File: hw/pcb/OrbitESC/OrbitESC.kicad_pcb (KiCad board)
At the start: 4 copper layers, 58 x 30 mm, 143 parts, among them J1 USB_C_Receptacle_USB2.0, J11 VDC, J12 GND, J3 TermA, J4 TermB, J5 TermC, J6 CAN1, Q1 MCAC80N10Y, Q2 MCAC80N10Y, Q3 MCAC80N10Y, Q4 MCAC80N10Y, Q5 MCAC80N10Y, Q6 MCAC80N10Y, Q7 2N7002, SW1 Reset, SW2 Boot, U1 TLE9250X, U10 CP2104, U11 STM32L432KBUx, U2 AT25SF081-SSHD-X, U3 24LC128, U4 74HC596, U5 DRV8300DRGER, U6 TSV994, U7 AP62200Z6-7, U8 AP2171W, U9 AP2120

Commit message: PCB cleanup
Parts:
- C10, C13, C4, C7, R15, R19, R20, R23, R24, U10: moved to F.Cu
- R9: moved to B.Cu
- moved D5 53.0 mm to (173.8, 71.3)
- moved D16 50.2 mm to (168.8, 69.4)
- moved D17 50.2 mm to (168.8, 71.7)
- moved D19 50.2 mm to (168.8, 74.0)
- moved R87 50.2 mm to (170.5, 69.4)
- moved R88 50.2 mm to (170.5, 71.7)
- moved R90 50.2 mm to (170.5, 74.0)
- moved SW2 42.4 mm to (155.2, 69.5)
- moved U2 41.8 mm to (156.0, 63.7)
- moved SW1 41.5 mm to (161.7, 70.6)
- moved R29 38.1 mm to (175.5, 74.0)
- moved D6 36.4 mm to (153.6, 103.3), turned to -90 degrees
- moved D7 35.4 mm to (152.1, 103.3), turned to -90 degrees
- moved D15 33.4 mm to (164.2, 65.0)
- moved D18 33.4 mm to (166.5, 65.0)
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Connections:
- U11 pad 10: /MCU/MOTOR_IB -> /MCU/MOTOR_IA
- U11 pad 11: /MCU/MOTOR_IC -> /MCU/MOTOR_IB
- U11 pad 13: /MCU/GATE_DRIVE_AL -> /MCU/GATE_DRIVE_CL
- U11 pad 15: /MCU/GATE_DRIVE_CL -> /MCU/GATE_DRIVE_AL
- U11 pad 18: /MCU/GATE_DRIVE_AH -> /MCU/GATE_DRIVE_CH
- U11 pad 20: /MCU/GATE_DRIVE_CH -> /MCU/GATE_DRIVE_AH
- U11 pad 7: /MCU/MOTOR_IA -> /MCU/MOTOR_IC
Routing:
- net GND: track 158.8 -> 45.7 mm, vias 27 -> 32
- net /Outputs and Shunts/SH_A: track 35.6 -> 13.7 mm
- net /MCU/INPUT_VOLTAGE: track 23.6 -> 1.85 mm
- net /Outputs and Shunts/SH_B: track 28.3 -> 13.3 mm, vias 11 -> 10
- net +3.3V: track 1.95 -> 15.9 mm
- net Net-(D6-Pad1): track 0.00 -> 7.87 mm
- net Net-(D7-Pad1): track 0.00 -> 5.00 mm
- net /Outputs and Shunts/SH_C: track 22.5 -> 18.2 mm
- net VBUS: track 17.3 -> 21.0 mm, vias 8 -> 9
- net /MCU/GATE_DRIVE_AL: track 0.00 -> 3.54 mm
- net /MCU/GATE_DRIVE_CL: track 0.00 -> 3.11 mm
- net SERIAL1_RST: track 0.00 -> 2.63 mm
- net /MCU/GATE_DRIVE_CH: track 0.00 -> 2.29 mm
- net /MCU/GATE_DRIVE_BL: track 0.00 -> 2.03 mm
- net /MCU/GATE_DRIVE_AH: track 0.00 -> 1.89 mm
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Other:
- board size 58 x 30 mm -> 42 x 30 mm
- board text removed: "BRK"
- board text removed: "CAN"
- board text removed: "DFU"
- board text removed: "RST"
- board text removed: "USR"

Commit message: More routing of components
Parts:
- C35, R62, U4: moved to B.Cu
- R7: moved to F.Cu
- moved D5 46.3 mm to (142.4, 105.3)
- moved D16 46.1 mm to (137.7, 103.4)
- moved R87 46.1 mm to (139.4, 103.4)
- moved D17 43.1 mm to (137.7, 101.5)
- moved R88 43.1 mm to (139.4, 101.5)
- moved R7 42.3 mm to (142.4, 103.4), turned to 0 degrees
- moved D18 41.6 mm to (137.7, 95.0), turned to 0 degrees
- moved D15 41.5 mm to (137.7, 96.9), turned to 0 degrees
- moved R90 40.3 mm to (139.4, 99.6)
- moved D19 40.3 mm to (137.7, 99.6)
- moved R89 39.1 mm to (139.4, 95.0), turned to -90 degrees
- moved R86 39.0 mm to (139.4, 96.9), turned to -90 degrees
- moved D20 37.2 mm to (137.7, 93.2), turned to 0 degrees
- moved R91 34.7 mm to (139.4, 93.2), turned to -90 degrees
- moved R62 33.2 mm to (140.0, 108.7), turned to -90 degrees
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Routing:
- net +5V: track 11.2 -> 36.7 mm, vias 6 -> 7
- net Net-(J6-Pad1): track 0.00 -> 10.1 mm
- net Net-(J6-Pad3): track 0.00 -> 4.92 mm
- net GND: track 45.7 -> 49.5 mm, vias 32 -> 33
- net +3.3V: track 15.9 -> 17.9 mm, vias 6 -> 7

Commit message: First draft of routed PCB
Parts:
- C1, R1, R3: moved to F.Cu
- C7: moved to B.Cu
- moved R29 41.2 mm to (138.2, 91.7), turned to 180 degrees
- moved R3 38.4 mm to (142.5, 101.6), turned to 180 degrees
- moved TP11 33.0 mm to (140.6, 91.7)
- moved SW2 31.7 mm to (142.0, 98.3), turned to -90 degrees
- moved R1 28.8 mm to (154.9, 102.1)
- moved TP10 26.8 mm to (156.3, 86.3)
- moved TP12 26.4 mm to (142.6, 91.7)
- moved C39 25.9 mm to (145.0, 98.5), turned to 90 degrees
- moved U2 23.5 mm to (151.7, 86.7)
- moved C1 22.7 mm to (153.9, 95.2), turned to 180 degrees
- moved TP9 20.4 mm to (156.9, 87.8)
- moved SW1 19.1 mm to (153.9, 98.3), turned to 90 degrees
- moved U3 17.7 mm to (142.2, 87.9), turned to -90 degrees
- moved R78 17.3 mm to (145.0, 87.6), turned to 180 degrees
- moved R70 17.1 mm to (147.1, 88.1)
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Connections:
- U11 pad 12: LED_nCS -> unconnected-(U11-Pad12)
- U11 pad 3: unconnected-(U11-Pad3) -> LED_nCS
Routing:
- net GND: track 49.5 -> 93.1 mm, vias 33 -> 45
- net NOR_MOSI: track 0.00 -> 42.3 mm, vias 0 -> 2
- net NOR_SCK: track 0.00 -> 41.4 mm, vias 0 -> 2
- net CAN1_TXD: track 0.00 -> 31.8 mm, vias 0 -> 1
- net CAN1_RXD: track 0.00 -> 30.8 mm, vias 0 -> 1
- net nRESET: track 0.00 -> 28.7 mm, vias 0 -> 1
- net NOR_nCS: track 0.00 -> 27.3 mm, vias 0 -> 2
- net NOR_MISO: track 0.00 -> 24.3 mm, vias 0 -> 2
- net +3.3V: track 17.9 -> 39.2 mm, vias 7 -> 16
- net SERIAL1_IN: track 0.00 -> 20.6 mm, vias 0 -> 2
- net LED_nCS: track 0.00 -> 19.6 mm, vias 0 -> 1
- net SERIAL1_OUT: track 0.00 -> 19.3 mm, vias 0 -> 2
- net /MCU/Status LEDs/CAN1_ACTV: track 0.00 -> 16.3 mm, vias 0 -> 1
- net /MCU/GATE_DRIVE_AH: track 1.89 -> 18.0 mm
- net EEPROM_SDA: track 0.00 -> 14.7 mm
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
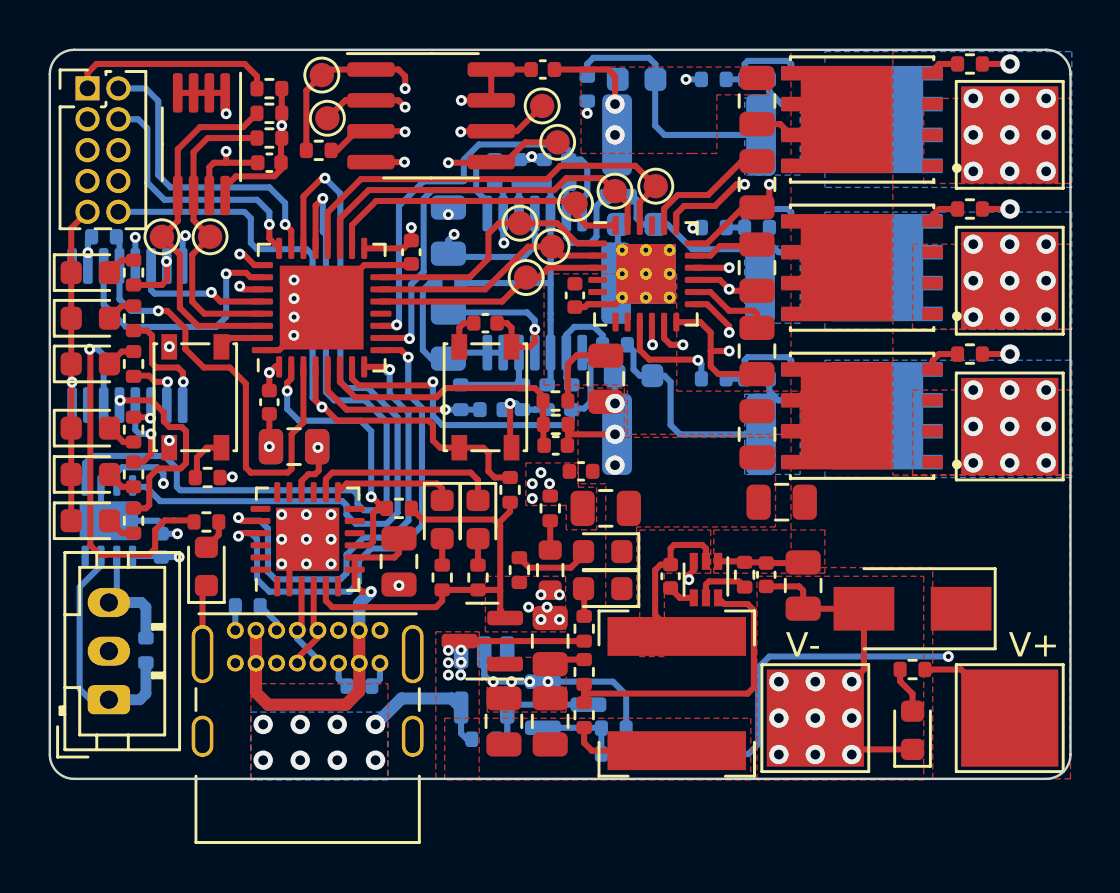
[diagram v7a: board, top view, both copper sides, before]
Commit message: Clean up DRC errors
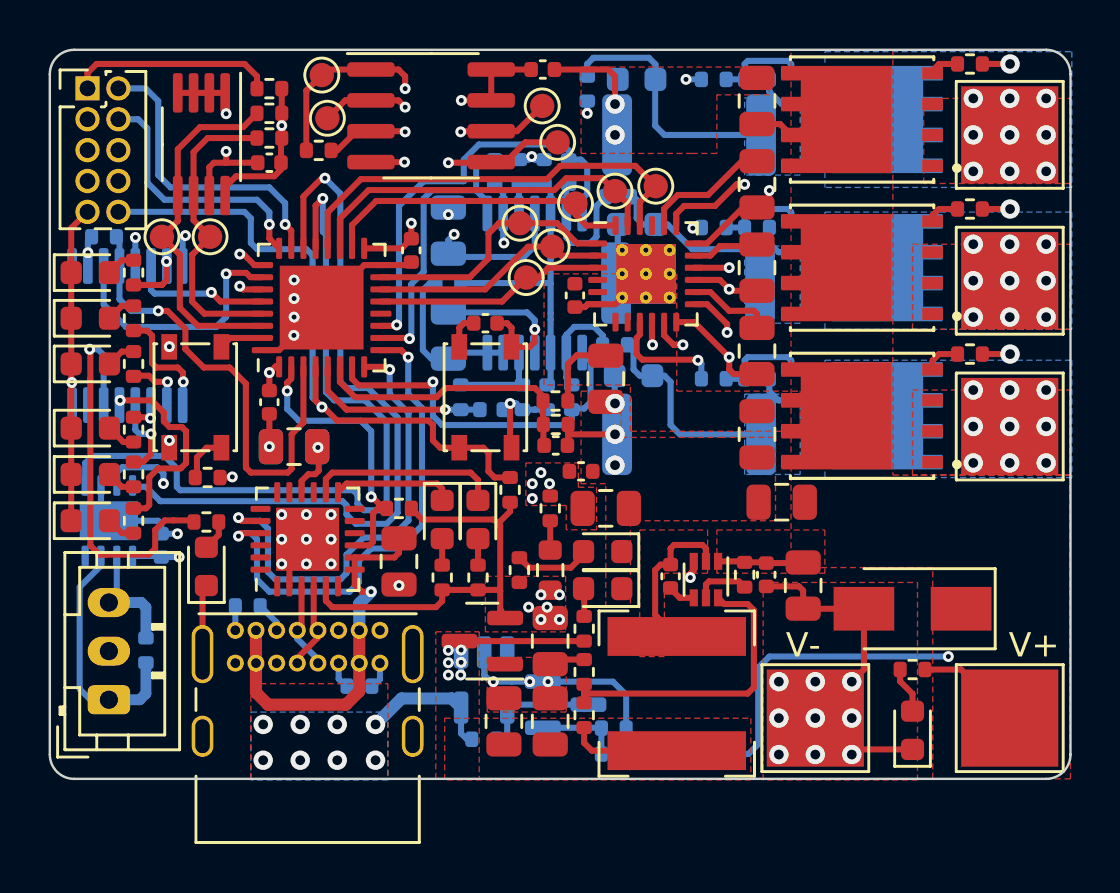
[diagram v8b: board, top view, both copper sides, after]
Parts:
- moved C41 0.08 mm to (150.9, 92.3)
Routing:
- net GND: track 93.1 -> 91.5 mm, vias 45 -> 44
- net /Outputs and Shunts/SH_C: track 18.2 -> 16.9 mm
